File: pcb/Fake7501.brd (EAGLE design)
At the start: 69.8 x 21 mm, 16 parts, among them IC2 XC9572XLTQG100, IC5 HDR, IC6 65(C)02

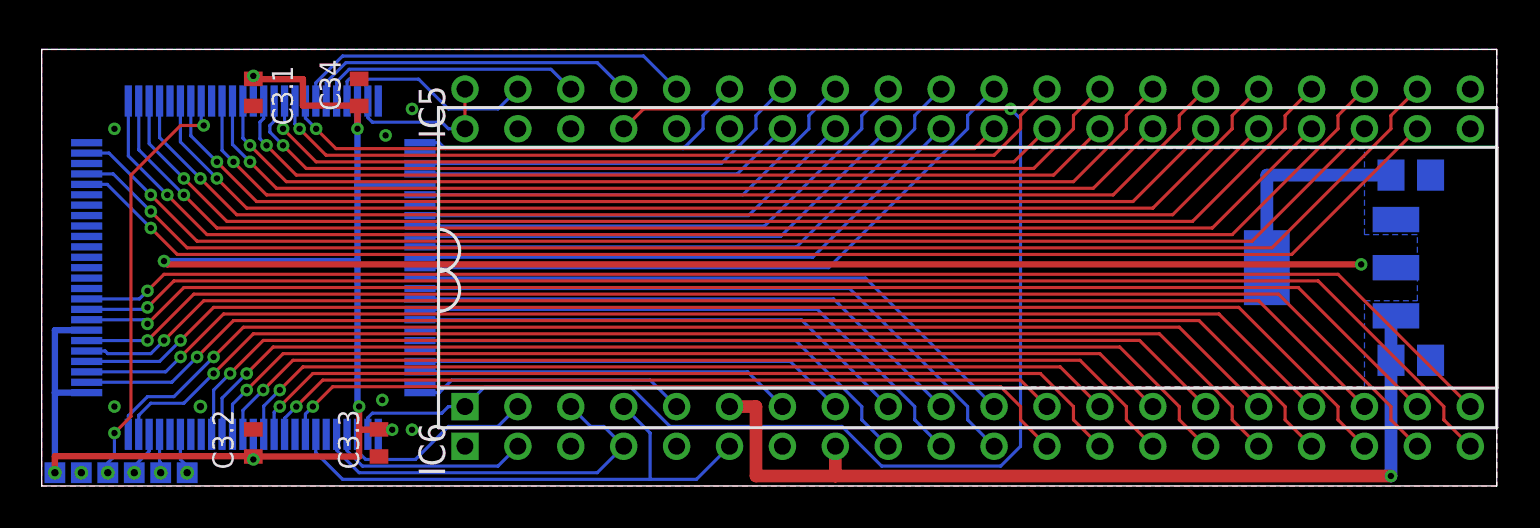
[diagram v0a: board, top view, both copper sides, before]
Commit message: Updated PCB to fix 7501 footprint errors Added GATE_IN functionality in hdl Added support for 65C02S
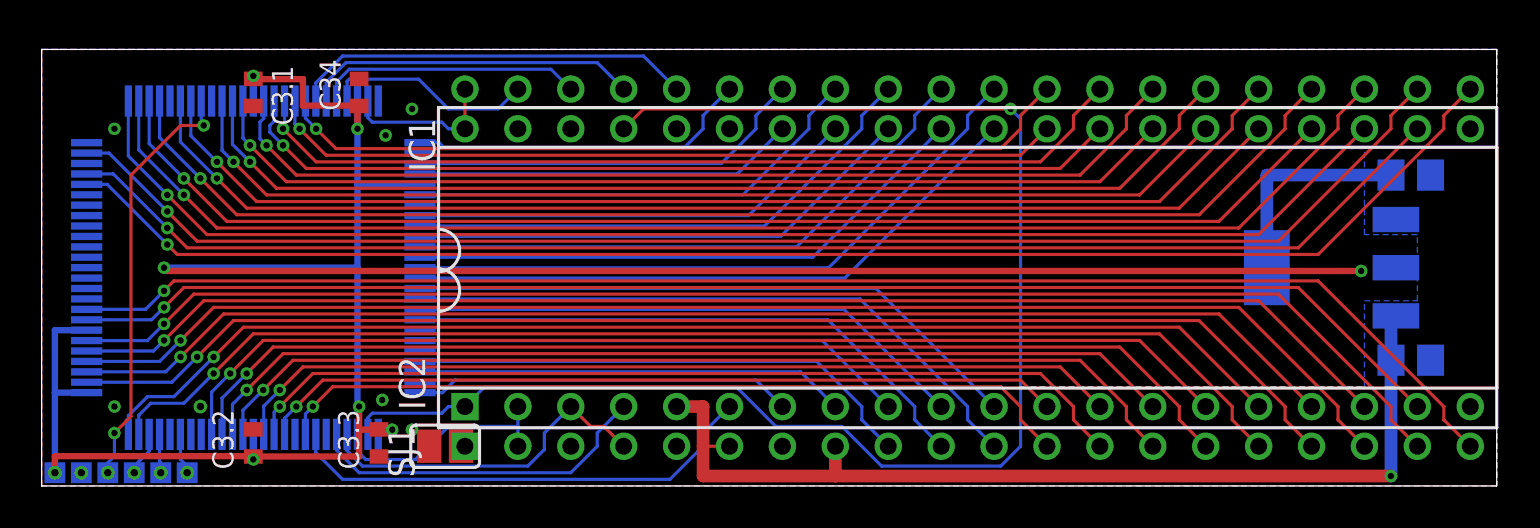
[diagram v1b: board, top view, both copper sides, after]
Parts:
- removed IC6: 65(C)02, commodore:DIL40-ROUNDPAD
- added IC3: XC9572XLTQG100, xilinx_xc95XXXxl:TQFP100
- added SJ1: (no value), jumper:SJ
- IC1: value HDR -> CSG7501
- IC2: value XC9572XLTQG100 -> W65C02SP; device xilinx_xc95XXXxl:TQFP100 -> commodore:DIL40-ROUNDPAD
- moved IC2 34.3 mm to (44.5, 9.53), flipped to the top
- renumbered IC5 to IC1
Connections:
- removed net !NMI: IC1.4, IC2.32, IC6.6
- removed net !RDY': IC2.29, IC6.2
- new net GATE_IN: IC1.23, IC3.77
- new net N$1: IC2.1, SJ1.2
- net !IRQ: now also IC2.4, IC3.29; no longer IC2.30, IC6.4
- net !RDY: now also IC2.2, IC3.28; no longer IC2.28
- net !RESET: now also IC2.40, IC3.99; no longer IC2.99, IC6.40
- net +3V3: now also IC3.26, IC3.38, IC3.5, IC3.51, IC3.57, IC3.88, IC3.98; no longer IC2.26, IC2.38, IC2.5, IC2.51, IC2.57, IC2.88, IC2.98
- net A'0: now also IC2.9, IC3.22; no longer IC2.20, IC6.9
- net A'1: now also IC2.10, IC3.18; no longer IC2.17, IC6.10
- net A'10: now also IC2.19, IC3.56; no longer IC2.56, IC6.19
- net A'11: now also IC2.20, IC3.59; no longer IC2.59, IC6.20
- net A'12: now also IC2.22, IC3.72; no longer IC2.71, IC6.22
- net A'13: now also IC2.23, IC3.76; no longer IC2.74, IC6.23
- net A'14: now also IC2.24, IC3.78; no longer IC2.77, IC6.24
- net A'15: now also IC2.25, IC3.81; no longer IC2.79, IC6.25
- net A'2: now also IC2.11, IC3.16; no longer IC2.15, IC6.11
- net A'3: now also IC2.12, IC3.33; no longer IC2.33, IC6.12
- net A'4: now also IC2.13, IC3.36; no longer IC2.36, IC6.13
- net A'5: now also IC2.14, IC3.39; no longer IC2.39, IC6.14
- net A'6: now also IC2.15, IC3.41; no longer IC2.41, IC6.15
- net A'7: now also IC2.16, IC3.49; no longer IC2.49, IC6.16
- net A'8: now also IC2.17, IC3.52; no longer IC2.52, IC6.17
- net A'9: now also IC2.18, IC3.54; no longer IC2.54, IC6.18
- net A0: now also IC1.6, IC3.32; no longer IC1.7, IC2.23
- net A1: now also IC1.7, IC3.25; no longer IC1.8, IC2.22
- net A10: now also IC1.16, IC3.50; no longer IC1.17, IC2.53
- net A11: now also IC1.17, IC3.53; no longer IC1.18, IC2.55
- net A12: now also IC1.18, IC3.55; no longer IC1.19, IC2.58
- net A13: now also IC1.19, IC3.58; no longer IC1.20, IC2.60
- net A14: now also IC1.21, IC3.71; no longer IC1.22, IC2.72
- net A15: now also IC1.22, IC3.74; no longer IC1.23, IC2.76
- net A2: now also IC1.8, IC3.23; no longer IC1.9, IC2.18
- net A3: now also IC1.9, IC3.20; no longer IC1.10, IC2.16
- net A4: now also IC1.10, IC3.17; no longer IC1.11, IC2.14
- net A5: now also IC1.11, IC3.15; no longer IC1.12, IC2.35
- net A6: now also IC1.12, IC3.35; no longer IC1.13, IC2.37
- net A7: now also IC1.13, IC3.37; no longer IC1.14, IC2.40
- net A8: now also IC1.14, IC3.40; no longer IC1.15, IC2.42
- net A9: now also IC1.15, IC3.42; no longer IC1.16, IC2.50
- net AEC: now also IC1.4, IC3.30; no longer IC1.5, IC2.25
- net D'0: now also IC2.33, IC3.8; no longer IC2.8, IC6.33
- net D'1: now also IC2.32, IC3.10; no longer IC2.10, IC6.32
- net D'2: now also IC2.31, IC3.12; no longer IC2.12, IC6.31
- net D'3: now also IC2.30, IC3.14; no longer IC2.93, IC6.30
- net D'4: now also IC2.29, IC3.92; no longer IC2.91, IC6.29
- net D'5: now also IC2.28, IC3.90; no longer IC2.89, IC6.28
- net D'6: now also IC2.27, IC3.87; no longer IC2.86, IC6.27
- net D'7: now also IC2.26, IC3.85; no longer IC2.82, IC6.26
- net D0: now also IC3.96; no longer IC2.96
- net D1: now also IC3.95; no longer IC2.95
- net D2: now also IC3.94; no longer IC2.94
- net D3: now also IC3.1; no longer IC2.1
- net D4: now also IC3.3; no longer IC2.3
- net D5: now also IC3.6; no longer IC2.6
- net D6: now also IC3.9; no longer IC2.9
- net D7: now also IC3.11; no longer IC2.11
- net GND: now also IC1.20, IC3.100, IC3.21, IC3.31, IC3.44, IC3.62, IC3.69, IC3.75, IC3.84, SJ1.1; no longer IC1.21, IC2.100, IC2.31, IC2.44, IC2.62, IC2.69, IC2.75, IC2.84, IC6.1, IC6.21
- net N$3: now also IC3.48; no longer IC2.48
- net N$4: now also IC3.47; no longer IC2.47
- net N$5: now also IC3.45; no longer IC2.45
- net N$6: now also IC3.83; no longer IC2.83
- net P0: now also IC3.13; no longer IC2.13
- net P1: now also IC3.93; no longer IC2.92
- net P2: now also IC3.91; no longer IC2.90
- net P3: now also IC3.89; no longer IC2.87
- net P4: now also IC3.86; no longer IC2.85
- net P5: now also IC3.82; no longer IC2.81
- net P6: now also IC3.79; no longer IC2.78
- net PHI: now also IC2.37, IC3.27; no longer IC2.27, IC6.37
- net R/!W: now also IC3.97; no longer IC2.97
- net R/!W': now also IC2.34, IC3.4; no longer IC2.4, IC6.34
- net VCC: now also IC1.5, IC2.6, IC2.8; no longer IC1.6, IC6.8
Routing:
- net GATE_IN: track 0.00 -> 65.9 mm, vias 0 -> 1
- net !NMI: track 25.9 -> 0.00 mm
- net !RDY': track 9.69 -> 0.00 mm
- net A5: track 38.7 -> 29.9 mm, vias 1 -> 0
- net A9: track 58.5 -> 52.1 mm
- net A0: track 18.1 -> 23.1 mm
- net A7: track 47.7 -> 43.1 mm
- net A6: track 43.1 -> 38.7 mm
- net A8: track 52.1 -> 47.7 mm
- net D'3: track 34.9 -> 30.5 mm, vias 1 -> 0
- net VCC: track 44.4 -> 48.3 mm
- net AEC: track 13.1 -> 16.7 mm
- net A2: track 24.2 -> 20.6 mm
- net A3: track 27.2 -> 23.8 mm
- net A10: track 61.8 -> 58.5 mm
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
